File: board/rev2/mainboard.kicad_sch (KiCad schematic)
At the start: 0 parts

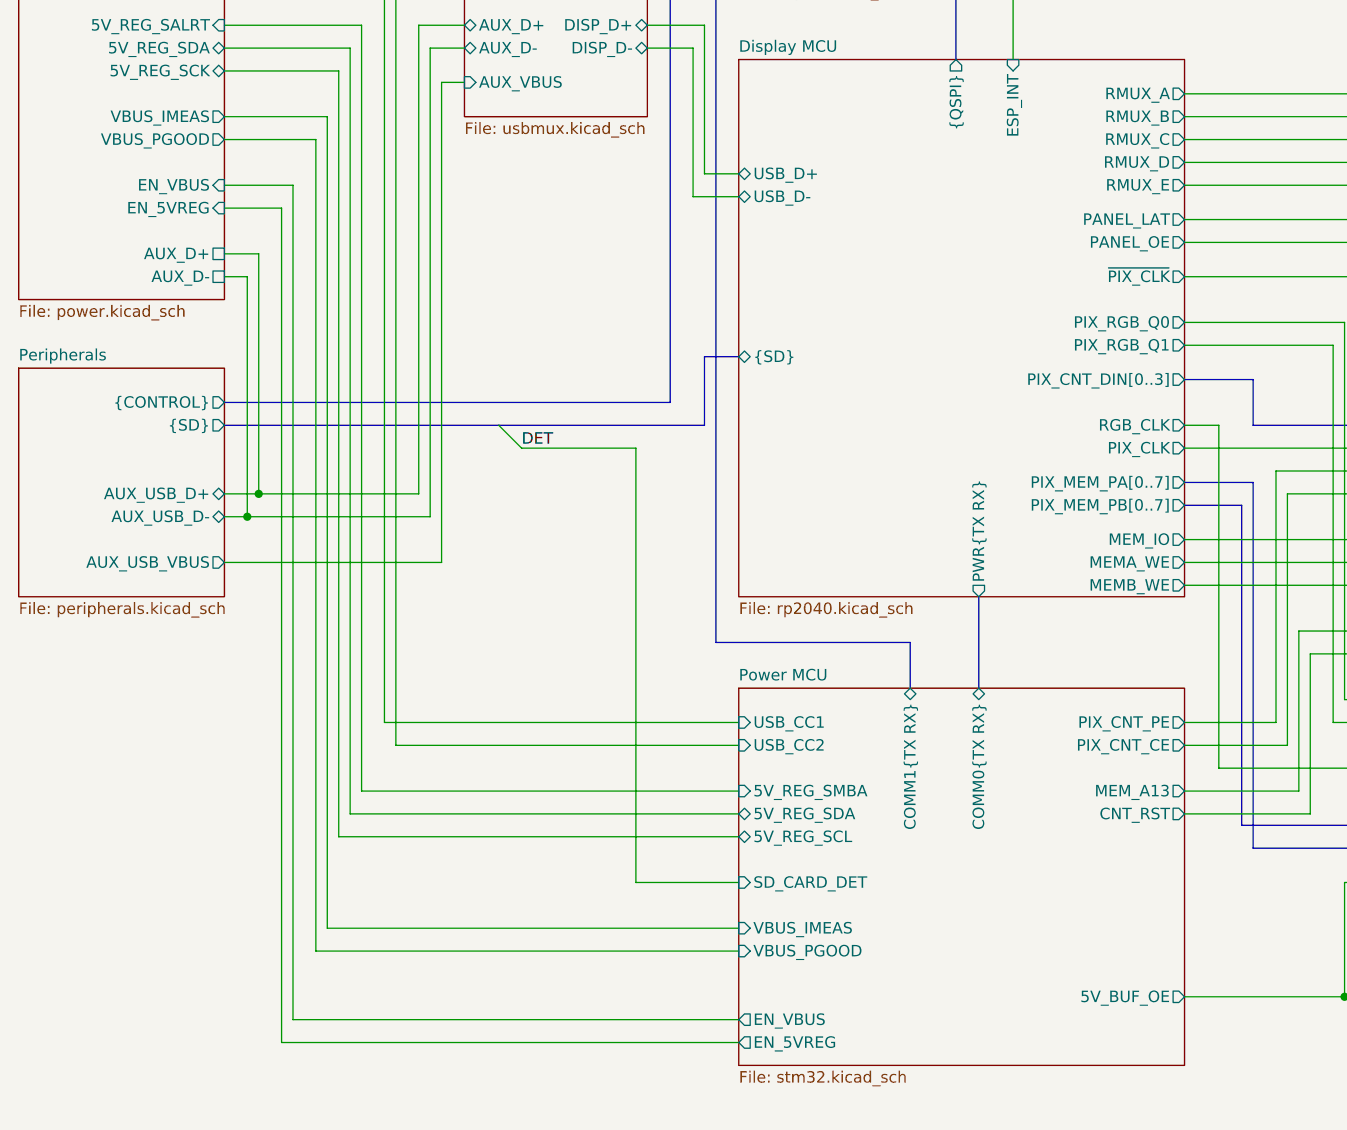
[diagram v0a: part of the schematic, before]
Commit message: Board REVB - fix 5V mux and add discharge path
also, fix a few routing issues
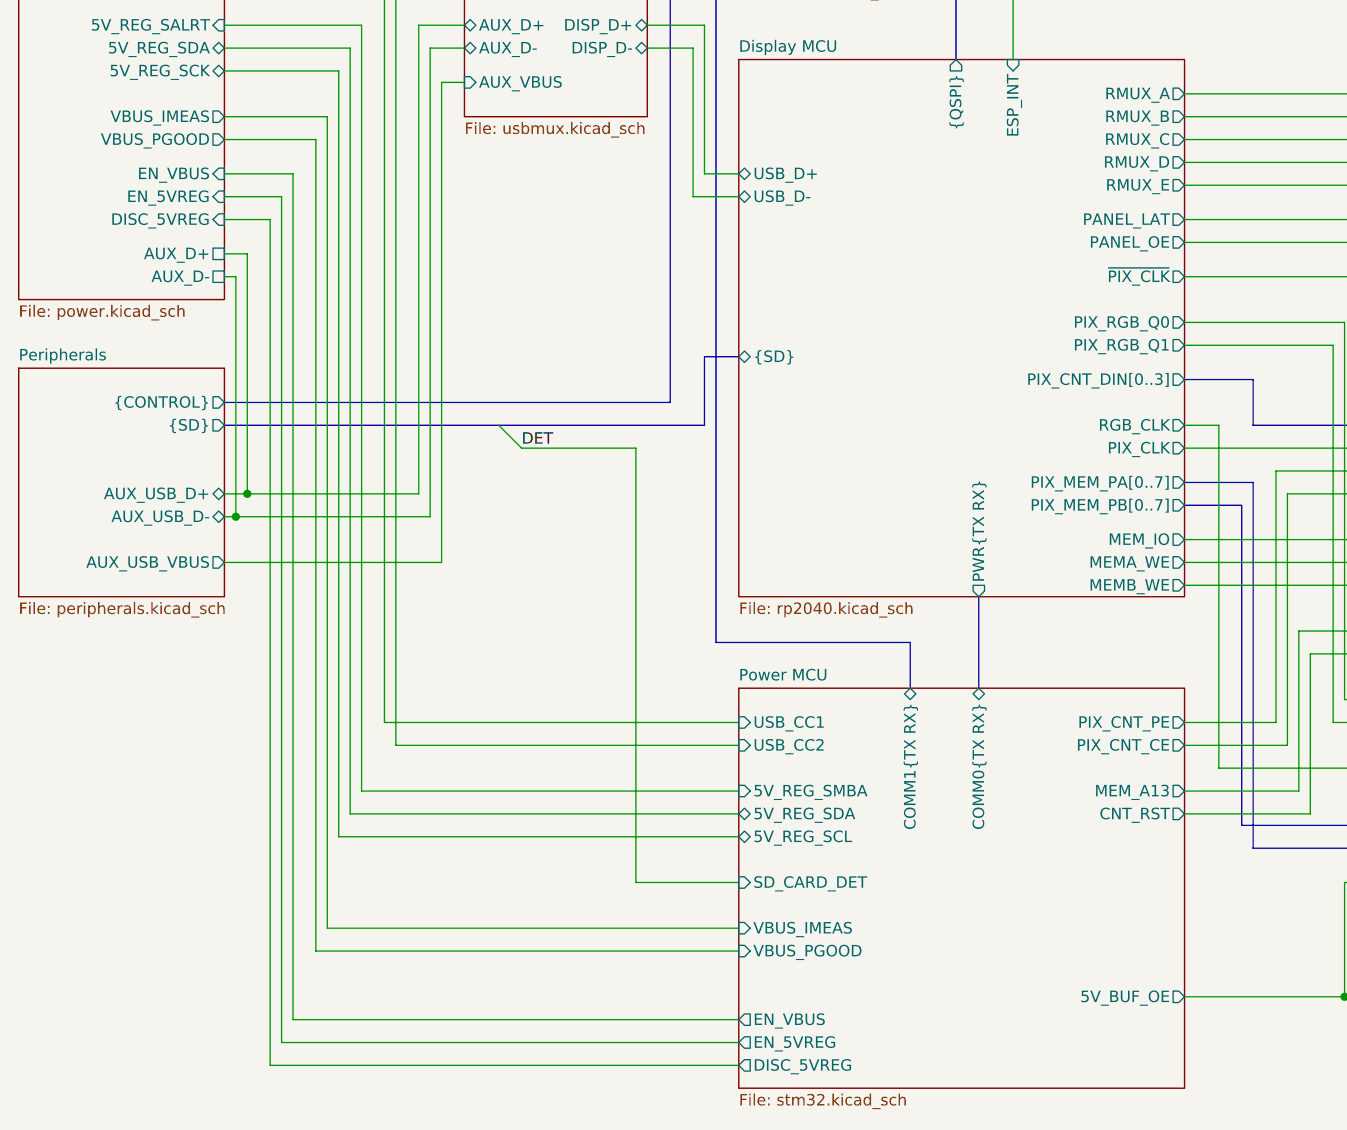
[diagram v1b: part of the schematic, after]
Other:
- sheet Power ports: added DISC_5VREG; removed none
- sheet Power MCU ports: added DISC_5VREG; removed none
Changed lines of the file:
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@@
+	)
+	(junction
+		(at 39.37 107.95)
+		(diameter 0)
+		(color 0 0 0 0)
 	)
 	(junction
@@
 	)
 	(junction
-		(at 41.91 105.41)
-		(diameter 0)
-		(color 0 0 0 0)
-	)
-	(junction
-		(at 40.64 107.95)
-		(diameter 0)
-		(color 0 0 0 0)
-	)
-	(junction
 		(at 226.06 57.15)
 		(diameter 0)
@@
 	)
 	(junction
+		(at 40.64 105.41)
+		(diameter 0)
+		(color 0 0 0 0)
+	)
+	(junction
 		(at 234.95 107.95)
 		(diameter 0)
@@
 	(wire
 		(pts
-			(xy 40.64 81.28) (xy 38.1 81.28)
-		)
-		(stroke
-			(width 0)
-			(type default)
-		)
-	)
-	(wire
-		(pts
-			(xy 45.72 71.12) (xy 38.1 71.12)
+			(xy 39.37 81.28) (xy 38.1 81.28)
+		)
+		(stroke
+			(width 0)
+			(type default)
+		)
+	)
+	(wire
+		(pts
+			(xy 45.72 69.85) (xy 38.1 69.85)
 		)
 		(stroke
@@
 	(wire
 		(pts
-			(xy 40.64 107.95) (xy 40.64 81.28)
+			(xy 39.37 107.95) (xy 39.37 81.28)
 		)
 		(stroke
@@
 	(wire
 		(pts
+			(xy 40.64 105.41) (xy 59.69 105.41)
+		)
+		(stroke
+			(width 0)
+			(type default)
+		)
+	)
+	(wire
+		(pts
 			(xy 144.78 71.12) (xy 203.2 71.12)
 		)
@@
 	(wire
 		(pts
-			(xy 41.91 105.41) (xy 59.69 105.41)
-		)
-		(stroke
-			(width 0)
-			(type default)
-		)
-	)
-	(wire
-		(pts
-			(xy 38.1 107.95) (xy 40.64 107.95)
+			(xy 38.1 107.95) (xy 39.37 107.95)
 		)
 		(stroke
@@
 	(wire
 		(pts
+			(xy 43.18 74.93) (xy 43.18 168.91)
+		)
+		(stroke
+			(width 0)
+			(type default)
+		)
+	)
+	(wire
+		(pts
 			(xy 200.66 57.15) (xy 226.06 57.15)
 		)
@@
 	(wire
 		(pts
-			(xy 41.91 105.41) (xy 41.91 78.74)
+			(xy 40.64 105.41) (xy 40.64 78.74)
 		)
 		(stroke
@@
 	(wire
 		(pts
-			(xy 40.64 107.95) (xy 60.96 107.95)
-		)
-		(stroke
-			(width 0)
-			(type default)
-		)
-	)
-	(wire
-		(pts
 			(xy 52.07 140.97) (xy 95.25 140.97)
 		)
@@
 	(wire
 		(pts
-			(xy 41.91 78.74) (xy 38.1 78.74)
+			(xy 40.64 78.74) (xy 38.1 78.74)
 		)
 		(stroke
@@
 	(wire
 		(pts
-			(xy 45.72 163.83) (xy 45.72 71.12)
+			(xy 45.72 163.83) (xy 45.72 69.85)
 		)
 		(stroke
@@
 	(wire
 		(pts
+			(xy 43.18 168.91) (xy 95.25 168.91)
+		)
+		(stroke
+			(width 0)
+			(type default)
+		)
+	)
+	(wire
+		(pts
 			(xy 237.49 116.84) (xy 226.06 116.84)
 		)
@@
 	(wire
 		(pts
+			(xy 39.37 107.95) (xy 60.96 107.95)
+		)
+		(stroke
+			(width 0)
+			(type default)
+		)
+	)
+	(wire
+		(pts
+			(xy 38.1 74.93) (xy 43.18 74.93)
+		)
+		(stroke
+			(width 0)
+			(type default)
+		)
+	)
+	(wire
+		(pts
 			(xy 201.93 68.58) (xy 201.93 59.69)
 		)
@@
 	(wire
 		(pts
-			(xy 38.1 105.41) (xy 41.91 105.41)
+			(xy 38.1 105.41) (xy 40.64 105.41)
 		)
 		(stroke
@@
 	(wire
 		(pts
-			(xy 44.45 73.66) (xy 38.1 73.66)
+			(xy 44.45 72.39) (xy 38.1 72.39)
 		)
 		(stroke
@@
 	(wire
 		(pts
-			(xy 44.45 166.37) (xy 44.45 73.66)
+			(xy 44.45 166.37) (xy 44.45 72.39)
 		)
 		(stroke
@@
 	(sheet
 		(at 95.25 127)
-		(size 49.53 41.91)
+		(size 49.53 44.45)
 		(exclude_from_sim no)
 		(in_bom yes)
@@
 		)
 		(property "Sheetfile" "stm32.kicad_sch"
-			(at 95.25 169.4946 0)
+			(at 95.25 172.0346 0)
 			(show_name no)
 			(do_not_autoplace no)
@@
 		(pin "SD_CARD_DET" input
 			(at 95.25 148.59 180)
+			(effects
+				(font
+					(size 1.27 1.27)
+				)
+				(justify left)
+			)
+		)
+		(pin "DISC_5VREG" output
+			(at 95.25 168.91 180)
 			(effects
 				(font
@@
 		)
 		(pin "EN_VBUS" input
-			(at 38.1 71.12 0)
+			(at 38.1 69.85 0)
 			(effects
 				(font
@@
 		)
 		(pin "EN_5VREG" input
-			(at 38.1 73.66 0)
+			(at 38.1 72.39 0)
 			(effects
 				(font
@@
 			(effects
 				(font
+					(size 1.27 1.27)
+				)
+				(justify right)
+			)
+		)
+		(pin "DISC_5VREG" input
+			(at 38.1 74.93 0)
+			(effects
+				(font
